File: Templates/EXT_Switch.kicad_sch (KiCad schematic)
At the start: 4 parts, among them K1 G6K-2F-Y_DC5, K2 HF32F-G-HS

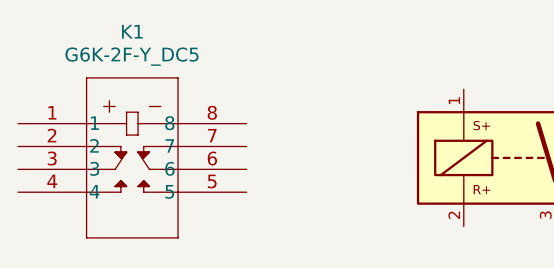
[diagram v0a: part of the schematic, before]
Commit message: update: 修复库文件缺失
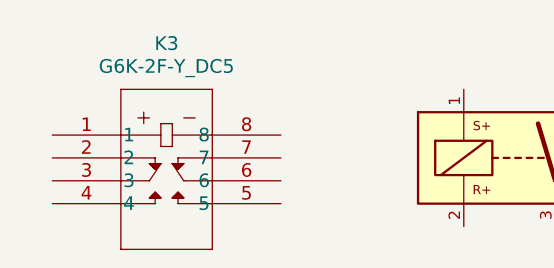
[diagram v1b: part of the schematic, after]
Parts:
- removed K1: G6K-2F-Y_DC5, DuRuofu_Switch:G6K-2F-Y DC5, symbol EXT_Switch:G6K-2F-Y_DC5
- added K3: G6K-2F-Y_DC5, EXT_Switch_SMD:G6K-2F-Y DC5, symbol EXT_Switch:G6K-2F-Y_DC5
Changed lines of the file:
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@@
 	)
 	(symbol
+		(lib_name "G6K-2F-Y_DC5_1")
 		(lib_id "EXT_Switch:G6K-2F-Y_DC5")
-		(at 31.75 49.53 0)
+		(at 35.56 50.8 0)
 		(unit 1)
 		(exclude_from_sim no)
@@
 		(dnp no)
 		(fields_autoplaced yes)
-		(property "Reference" "K1"
-			(at 44.45 39.37 0)
+		(property "Reference" "K3"
+			(at 48.26 40.64 0)
 			(effects
 				(font
@@
 		)
 		(property "Value" "G6K-2F-Y_DC5"
-			(at 44.45 41.91 0)
+			(at 48.26 43.18 0)
 			(effects
 				(font
@@
 			)
 		)
-		(property "Footprint" "DuRuofu_Switch:G6K-2F-Y DC5"
-			(at 45.085 43.434 0)
+		(property "Footprint" "EXT_Switch_SMD:G6K-2F-Y DC5"
+			(at 48.895 44.704 0)
 			(effects
 				(font
@@
 		)
 		(property "Datasheet" ""
-			(at 31.75 49.53 0)
+			(at 35.56 50.8 0)
 			(effects
 				(font
@@
 		)
 		(property "Description" "信号继电器，高达 2 A"
-			(at 31.75 49.53 0)
+			(at 35.56 50.8 0)
 			(effects
 				(font
@@
 		(pin "1"
 		)
-		(pin "2"
-		)
-		(pin "6"
+		(pin "8"
 		)
 		(pin "7"
+		)
+		(pin "2"
 		)
 		(pin "3"
@@
 		(pin "5"
 		)
-		(pin "8"
+		(pin "6"
 		)
 		(instances
 			(project ""
 				(path "/15ae7a0d-a53d-4804-b6bf-a747840a1ecc/f29c734e-aa56-454c-b180-722885d553d3"
-					(reference "K1")
+					(reference "K3")
 					(unit 1)
 				)
